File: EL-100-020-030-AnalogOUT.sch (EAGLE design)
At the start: 38 parts, among them U16 24AA256-I/SN, U17 SW-DIL-3, U3 LMR62421XSD, U4 OPA2170AID, U5 LTC2635HUD-LMI10PBF

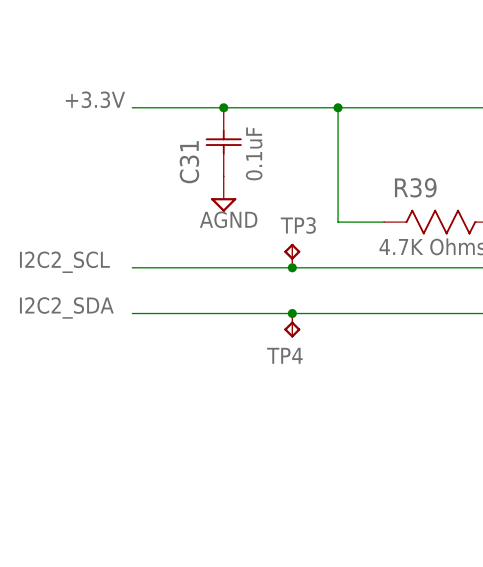
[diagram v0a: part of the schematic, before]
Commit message: DIN rail PT1000 and indicator
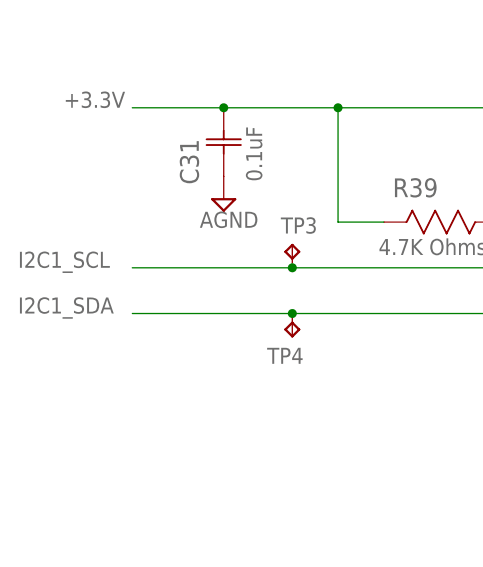
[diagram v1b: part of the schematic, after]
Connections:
- new net I2C1_SCL: TP3.TP, U5.SCL
- new net I2C1_SDA: TP4.TP, U5.SDA
- net I2C2_SCL: no longer TP3.TP, U5.SCL
- net I2C2_SDA: no longer TP4.TP, U5.SDA
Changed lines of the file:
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@@
 <label x="241.3" y="50.8" size="1.778" layer="95"/>
-</segment>
-<segment>
-<pinref part="U5" gate="A" pin="SCL"/>
-<wire x1="99.06" y1="144.78" x2="73.66" y2="144.78" width="0.1524" layer="91"/>
-<wire x1="73.66" y1="144.78" x2="73.66" y2="142.24" width="0.1524" layer="91"/>
-<wire x1="73.66" y1="142.24" x2="45.72" y2="142.24" width="0.1524" layer="91"/>
-<label x="15.24" y="142.24" size="1.778" layer="95"/>
-<pinref part="TP3" gate="G$1" pin="TP"/>
-<wire x1="45.72" y1="142.24" x2="27.94" y2="142.24" width="0.1524" layer="91"/>
-<junction x="45.72" y="142.24"/>
 </segment>
 </net>
@@
 <wire x1="208.28" y1="53.34" x2="238.76" y2="53.34" width="0.1524" layer="91"/>
 <label x="241.3" y="53.34" size="1.778" layer="95"/>
-</segment>
-<segment>
-<pinref part="U5" gate="A" pin="SDA"/>
-<wire x1="99.06" y1="142.24" x2="76.2" y2="142.24" width="0.1524" layer="91"/>
-<wire x1="76.2" y1="142.24" x2="76.2" y2="137.16" width="0.1524" layer="91"/>
-<wire x1="76.2" y1="137.16" x2="45.72" y2="137.16" width="0.1524" layer="91"/>
-<label x="15.24" y="137.16" size="1.778" layer="95"/>
-<pinref part="TP4" gate="G$1" pin="TP"/>
-<wire x1="45.72" y1="137.16" x2="27.94" y2="137.16" width="0.1524" layer="91"/>
-<junction x="45.72" y="137.16"/>
 </segment>
 </net>
@@
 </segment>
 </net>
+<net name="I2C1_SCL" class="0">
+<segment>
+<pinref part="U5" gate="A" pin="SCL"/>
+<wire x1="99.06" y1="144.78" x2="73.66" y2="144.78" width="0.1524" layer="91"/>
+<wire x1="73.66" y1="144.78" x2="73.66" y2="142.24" width="0.1524" layer="91"/>
+<wire x1="73.66" y1="142.24" x2="45.72" y2="142.24" width="0.1524" layer="91"/>
+<label x="15.24" y="142.24" size="1.778" layer="95"/>
+<pinref part="TP3" gate="G$1" pin="TP"/>
+<wire x1="45.72" y1="142.24" x2="27.94" y2="142.24" width="0.1524" layer="91"/>
+<junction x="45.72" y="142.24"/>
+</segment>
+</net>
+<net name="I2C1_SDA" class="0">
+<segment>
+<pinref part="U5" gate="A" pin="SDA"/>
+<wire x1="99.06" y1="142.24" x2="76.2" y2="142.24" width="0.1524" layer="91"/>
+<wire x1="76.2" y1="142.24" x2="76.2" y2="137.16" width="0.1524" layer="91"/>
+<wire x1="76.2" y1="137.16" x2="45.72" y2="137.16" width="0.1524" layer="91"/>
+<label x="15.24" y="137.16" size="1.778" layer="95"/>
+<pinref part="TP4" gate="G$1" pin="TP"/>
+<wire x1="45.72" y1="137.16" x2="27.94" y2="137.16" width="0.1524" layer="91"/>
+<junction x="45.72" y="137.16"/>
+</segment>
+</net>

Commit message: prototype order status
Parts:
- removed C14: 220pF 50V, Kemet_By_element14_Batch_1:C0603C221J5GACTU
- removed C23: 22nF 50V, Kemet_By_element14_Batch_1:C0603C223K5RACTU
- removed C30, C31, C32, C48: 0.1uF, Kemet_By_element14_Batch_1:C0603C104K5RAC-TU
- removed C33, C34: 1000pF 1kV, supply2:C1206C102KDRACTU
- removed R26: 86.6K Ohms, Vishay_By_element14_Batch_1:CRCW060386K6FKEA
- removed R27: 10.2K Ohms, Vishay_By_element14_Batch_1:CRCW060310K2FKEA
- removed R29: 1 MOhms, Vishay_By_element14_Batch_1:CRCW06031M00FKEA
- removed R31, R38: 5.1K Ohms, Vishay_By_element14_Batch_1:CRCW06035K10FKEA
- removed R32, R33: 15K Ohms, Vishay_By_element14_Batch_1:CRCW060315K0FKEA
- removed R39, R82, R84, R85: 4.7K Ohms, Vishay_By_element14_Batch_1:CRCW06034K70FKEA
- removed R83: 10K Ohms, Vishay_By_element14_Batch_1:CRCW060310K0FKEA
- removed RV2, RV3: (no value), WE-VS:WE-VS-82536140_0603
- removed TP1, TP2, TP3, TP4, TP5: TPB1,27, testpad:TPB1,27
- removed U16: 24AA256-I/SN, Microchip_By_element14_Batch_1:24AA256-I/SN
- removed U17: SW-DIL-3, strasys_standard:SW-DIL-3
- added C1, C10, C2, C3, C6: 100nF, Kemet_By_element14_1:C0805C104K5RACTU
- added C4, C5, C7, C8: 0.082µF, Kemet_By_element14_1:C0805C180J5GACTU
- added C41: 220pF, Kemet_By_element14_1:C0805C221J5GACTU
- added C43: 22nF, Kemet_By_element14_1:C0805C223K5RACTU
- added R1, R2, R28, R3, R30, R4, R5, R6: 10K Ohms, Vishay_By_element14_Batch_1:CRCW080510K0JNEA
- added R10, R12, R14, R16, R17, R18, R7, R8: 1K Ohms, Vishay_By_element14_Batch_1:CRCW08051K00FKEA
- added R11, R13, R15, R9: 3K Ohms, Vishay_By_element14_Batch_1:CRCW080530K0FKEA
- added R42: 10.2K Ohms, Vishay_By_element14_Batch_1:CRCW080510K2FKEA
- added U1: LTC2635HMSE-LMI12PBF, strasys_standard:LTC2635HMSE-LMI12PBF
- added U6: LMR62421XMF, strasys_standard:LMR62421XMF
- added X1, X2: 944-12-08-00, strasys_standard:944-12-08-00
- added X3: 9012-26, con-WuP:9012-26
- C40: value 10uF 10V -> 10uF
- C42: value 10uF 25V -> 10uF
- R40: value 1K Ohms -> 1M Ohms; device Vishay_By_element14_Batch_1:CRCW06031K00FKEA -> Vishay_By_element14_Batch_1:CRCW08051M00FKTB
- R41: value 1K Ohms -> 86.6K Ohms; device Vishay_By_element14_Batch_1:CRCW06031K00FKEA -> Vishay_By_element14_Batch_1:CRCW080586K6FKEA
- U3: value LMR62421XSD -> OPA2170AID; device strasys_standard:LMR62421XSD -> strasys_standard:OPA2170AID; OC_FARNELL 2064679 -> (none)
- U5: value LTC2635HUD-LMI10PBF -> 24AA256-I/SN; device strasys_standard:LTC2635HUD-LMI10PBF -> Microchip_By_element14_Batch_1:24AA256-I/SN; MF LINEAR TECHNOLOGY -> MICROCHIP
- renumbered C12 to C40, C13 to C42, U4 to U2
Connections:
- removed net 24AA_A0: R85.2, U16.A0, U17.3
- removed net DGND: C23.C1, C40.C1, C42.C1, C48.C1, R27.2, U16.VSS, U17.4, U17.5, U17.6, U3.AGND, U3.DAP, U3.PGND
- removed net LDAC: R39.1, U5.~LDAC
- removed net N$19: R82.2, U16.A2
- removed net N$50: C32.C2, U5.REF
- removed net PE: C33.C1, C34.C1
- removed net SGND_A: RV2.1, RV3.1
- removed net VDD5V_F: C40.C2, L1.1, R29.2, U3.VIN
- new net 24AA-A0: R2.2, U5.A0, X2.2
- new net 24AA_A2: R4.2, U5.A2, X2.6
- new net AOUT3_0-10V: C8.C2, R17.1, X3.A2
- new net AOUT4_0-10V: C7.C2, R18.1, X3.B2
- new net CA0: U1.CA0, X1.2, X1.4, X1.6
- new net N$2: C2.C2, U1.REF
- new net OPA21_-IN_A1: R10.2, R9.1, U3.-IN_A
- new net OPA21_-IN_B1: R11.1, R12.2, U3.-IN_B
- new net OPA21_AOUTB1: R11.2, R18.2, U3.OUT_B
- new net OPA21_OUT_A1: R17.2, R9.2, U3.OUT_A
- new net SYS5V_F: C1.C2, C40.C2, L1.1, R40.2, U1.VCC, U6.VIN, X1.5, X3.A3
- new net VOUTC: U1.VOUTC, U3.+IN_A
- new net VOUTD: U1.VOUTD, U3.+IN_B
- net +12V: now also C3.C2, C41.C2, C43.C2, C6.C2, R41.1, U3.V+; no longer C14.C2, C23.C2, C30.C2, R26.1, TP5.TP
- net +3.3V: now also C10.C2, R1.1, R2.1, R28.1, R3.1, R30.1, R4.1, R5.1, R6.1, X3.A4; no longer C31.C2, C48.C2, R39.2, R82.1, R83.1, R84.1, R85.1, U16.VCC
- net 24AA_A1: now also R3.2, U5.A1, X2.4; no longer R84.2, U16.A1, U17.2
- net 24AA_WP: now also R30.2, U5.WP, X2.8; no longer R83.2, U16.WP, U17.1
- net AGND: now also C1.C1, C10.C1, C2.C1, C3.C1, C4.C1, C40.C1, C42.C1, C43.C1, C5.C1, C6.C1, C7.C1, C8.C1, R10.1, R12.1, R14.1, R16.1, R42.2, U1.GND, U1.GND_2, U3.V-, U5.VSS, U6.GND, X1.1, X2.1, X2.3, X2.5, X2.7, X3.B3, X3.B4; no longer C30.C1, C31.C1, C32.C1, R31.1, R38.1, U5.CA0, U5.CA1, U5.CA2, U5.GND, U5.GND_2, U5.REFLO
- net AOUT1_0-10V: now also C5.C2, R7.1, X3.A1; no longer C34.C2, R40.1, RV3.2
- net AOUT2_0-10V: now also C4.C2, R8.1, X3.B1; no longer C33.C2, R41.1, RV2.2
- net FB_LMR62: now also C41.C1, R41.2, R42.1, U6.FB; no longer C14.C1, R26.2, R27.1, U3.FB
- net I2C1_SCL: now also R6.2, U1.SCL, X3.A6; no longer TP3.TP, U5.SCL
- net I2C1_SDA: now also R5.2, U1.SDA, X3.A5; no longer TP4.TP, U5.SDA
- net I2C2_SCL: now also R1.2, U5.SCL, X3.B6; no longer U16.SCL
- net I2C2_SDA: now also R28.2, U5.SDA, X3.B5; no longer U16.SDA
- net N$39: now also R40.1, U6.EN; no longer R29.1, U3.EN
- net OPA21_-IN_A: now also R13.1, R14.2; no longer R31.2, R32.2
- net OPA21_-IN_B: now also R15.1, R16.2; no longer R33.2, R38.2
- net OPA21_AOUTB: now also R15.2, R8.2; no longer R33.1, R41.2
- net OPA21_OUT_A: now also R13.2, R7.2; no longer R32.1, R40.2
- net SW_LMR62: now also U6.SW; no longer U3.SW
- net VOUTA: now also U1.VOUTA; no longer TP2.TP, U5.VOUTA
- net VOUTB: now also U1.VOUTB; no longer TP1.TP, U5.VOUTB
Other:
- note added: "CA0 = GND: b0010000 = h10 CA0 = FLOAT: b0010001 = h11 CA0 = VCC: b0010010 = h12"
- note added: "Set I2C slave address: b01010 A2 A1 A0"
- note removed: "I2C slave address: b0010000 = h10"
- note removed: "I2C slave address: b1010100 = h54"

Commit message: production status
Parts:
- R17, R18, R7, R8: device Vishay_By_element14_Batch_1:CRCW08051K00FKEA -> Vishay_By_element14_Batch_1:CRCW08051K00JNEA
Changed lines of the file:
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@@
 <attribute name="TOLERANCE" value="±0.1%"/>
 </part>
-<part name="R7" library="Vishay_By_element14_Batch_1" deviceset="CRCW08051K00FKEA" device="" value="1K Ohms"/>
-<part name="R8" library="Vishay_By_element14_Batch_1" deviceset="CRCW08051K00FKEA" device="" value="1K Ohms"/>
+<part name="R7" library="Vishay_By_element14_Batch_1" deviceset="CRCW08051K00JNEA" device="" value="1K Ohms"/>
+<part name="R8" library="Vishay_By_element14_Batch_1" deviceset="CRCW08051K00JNEA" device="" value="1K Ohms"/>
 <part name="C4" library="Kemet_By_element14_1" deviceset="C0805C180J5GACTU" device="" value="0.082µF">
 <attribute name="MF" value=""/>
@@
 <attribute name="TOLERANCE" value="±0.1%"/>
 </part>
-<part name="R17" library="Vishay_By_element14_Batch_1" deviceset="CRCW08051K00FKEA" device="" value="1K Ohms"/>
-<part name="R18" library="Vishay_By_element14_Batch_1" deviceset="CRCW08051K00FKEA" device="" value="1K Ohms"/>
+<part name="R17" library="Vishay_By_element14_Batch_1" deviceset="CRCW08051K00JNEA" device="" value="1K Ohms"/>
+<part name="R18" library="Vishay_By_element14_Batch_1" deviceset="CRCW08051K00JNEA" device="" value="1K Ohms"/>
 <part name="C7" library="Kemet_By_element14_1" deviceset="C0805C180J5GACTU" device="" value="0.082µF">
 <attribute name="MF" value=""/>
